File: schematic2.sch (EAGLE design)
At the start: 76 parts, among them IC6 DS3231/SO

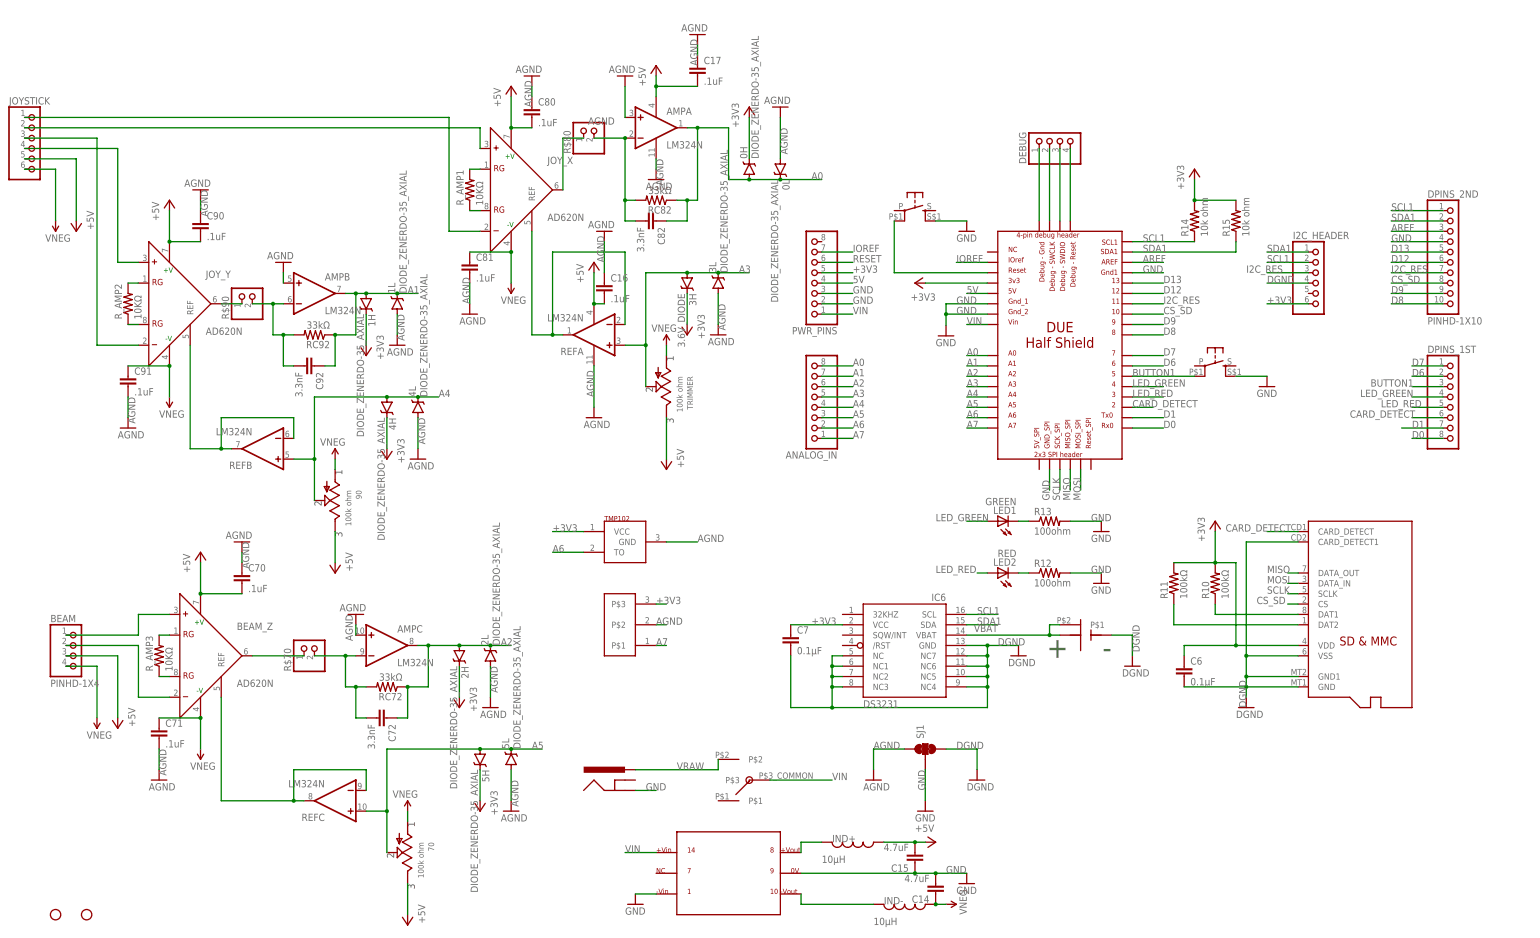
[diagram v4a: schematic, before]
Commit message: Added three separate ground pours for DGND, AGND, and GND.
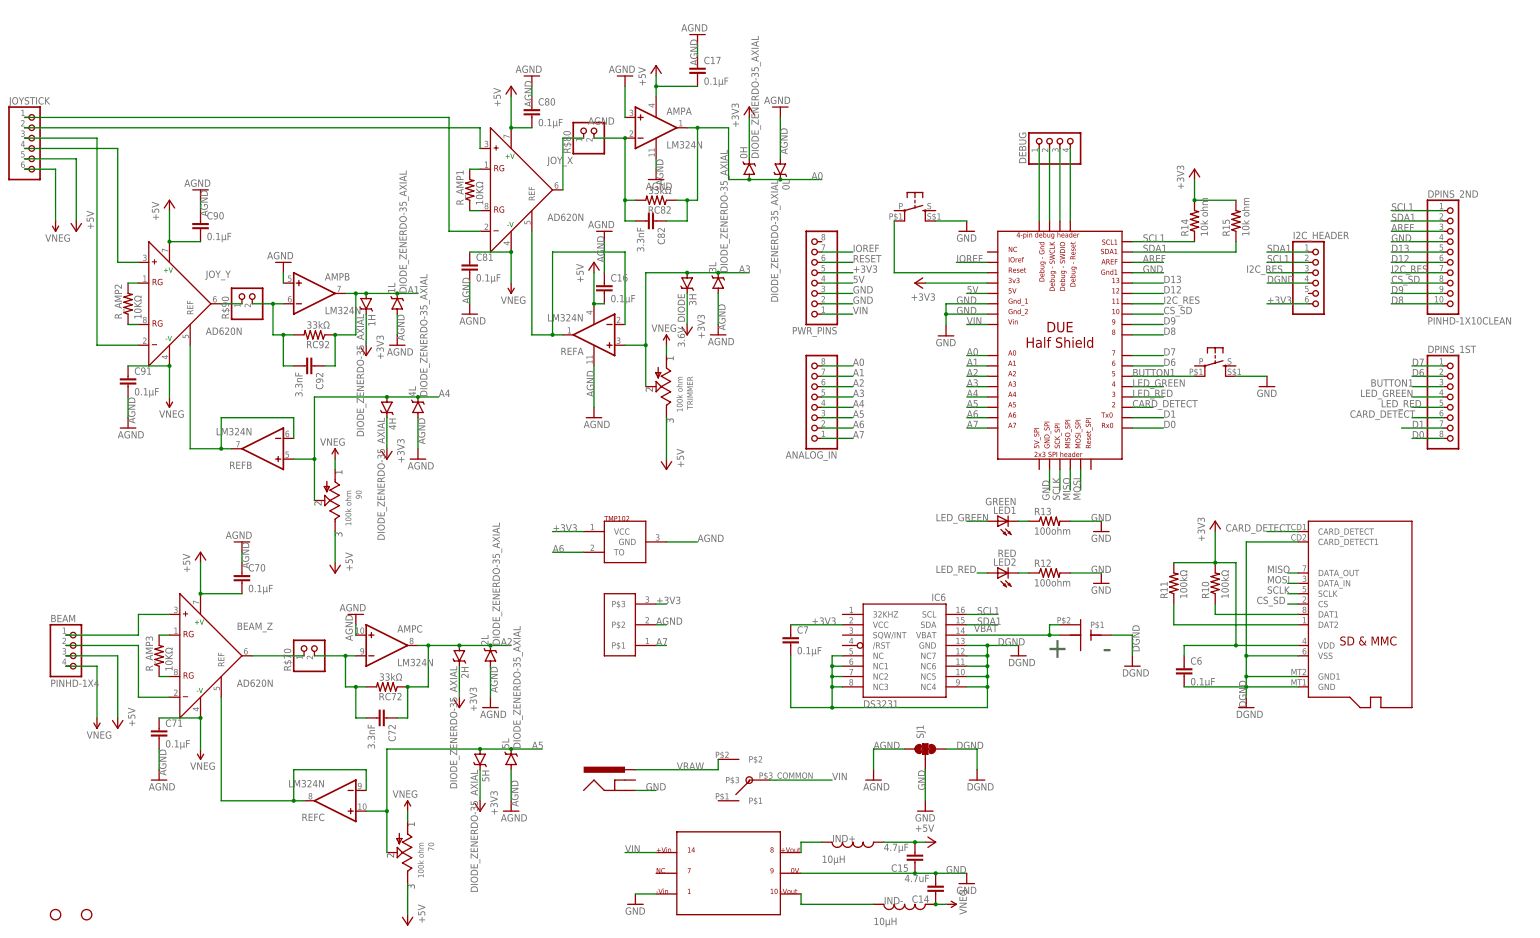
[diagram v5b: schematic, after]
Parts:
- C15: value 4.7uF -> 4.7µF
- C16, C17, C70, C71, C80, C81, C90, C91: value .1uF -> 0.1µF
- DPINS_2ND: value PINHD-1X10 -> PINHD-1X10CLEAN; device Felicia_force_logger:PINHD-1X10 -> Felicia_force_logger:PINHD-1X10CLEAN
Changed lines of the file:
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@@
 <grid distance="0.1" unitdist="inch" unit="inch" style="lines" multiple="1" display="no" altdistance="0.01" altunitdist="inch" altunit="inch"/>
 <layers>
-<layer number="1" name="Top" color="4" fill="1" visible="no" active="no"/>
-<layer number="16" name="Bottom" color="1" fill="1" visible="no" active="no"/>
-<layer number="17" name="Pads" color="2" fill="1" visible="no" active="no"/>
-<layer number="18" name="Vias" color="2" fill="1" visible="no" active="no"/>
-<layer number="19" name="Unrouted" color="6" fill="1" visible="no" active="no"/>
-<layer number="20" name="Dimension" color="15" fill="1" visible="no" active="no"/>
-<layer number="21" name="tPlace" color="7" fill="1" visible="no" active="no"/>
-<layer number="22" name="bPlace" color="7" fill="1" visible="no" active="no"/>
-<layer number="23" name="tOrigins" color="15" fill="1" visible="no" active="no"/>
-<layer number="24" name="bOrigins" color="15" fill="1" visible="no" active="no"/>
-<layer number="25" name="tNames" color="7" fill="1" visible="no" active="no"/>
-<layer number="26" name="bNames" color="7" fill="1" visible="no" active="no"/>
-<layer number="27" name="tValues" color="7" fill="1" visible="no" active="no"/>
-<layer number="28" name="bValues" color="7" fill="1" visible="no" active="no"/>
+<layer number="1" name="Top" color="4" fill="1" visible="yes" active="no"/>
+<layer number="16" name="Bottom" color="1" fill="1" visible="yes" active="no"/>
+<layer number="17" name="Pads" color="2" fill="1" visible="yes" active="no"/>
+<layer number="18" name="Vias" color="2" fill="1" visible="yes" active="no"/>
+<layer number="19" name="Unrouted" color="6" fill="1" visible="yes" active="no"/>
+<layer number="20" name="Dimension" color="15" fill="1" visible="yes" active="no"/>
+<layer number="21" name="tPlace" color="16" fill="1" visible="yes" active="no"/>
+<layer number="22" name="bPlace" color="14" fill="1" visible="yes" active="no"/>
+<layer number="23" name="tOrigins" color="15" fill="1" visible="yes" active="no"/>
+<layer number="24" name="bOrigins" color="15" fill="1" visible="yes" active="no"/>
+<layer number="25" name="tNames" color="7" fill="1" visible="yes" active="no"/>
+<layer number="26" name="bNames" color="7" fill="1" visible="yes" active="no"/>
+<layer number="27" name="tValues" color="7" fill="1" visible="yes" active="no"/>
+<layer number="28" name="bValues" color="7" fill="1" visible="yes" active="no"/>
 <layer number="29" name="tStop" color="7" fill="3" visible="no" active="no"/>
 <layer number="30" name="bStop" color="7" fill="6" visible="no" active="no"/>
@@
 <layer number="35" name="tGlue" color="7" fill="4" visible="no" active="no"/>
 <layer number="36" name="bGlue" color="7" fill="5" visible="no" active="no"/>
-<layer number="37" name="tTest" color="7" fill="1" visible="no" active="no"/>
-<layer number="38" name="bTest" color="7" fill="1" visible="no" active="no"/>
+<layer number="37" name="tTest" color="7" fill="1" visible="yes" active="no"/>
+<layer number="38" name="bTest" color="7" fill="1" visible="yes" active="no"/>
 <layer number="39" name="tKeepout" color="4" fill="11" visible="no" active="no"/>
 <layer number="40" name="bKeepout" color="1" fill="11" visible="no" active="no"/>
@@
 <layer number="44" name="Drills" color="7" fill="1" visible="no" active="no"/>
 <layer number="45" name="Holes" color="7" fill="1" visible="no" active="no"/>
-<layer number="46" name="Milling" color="3" fill="1" visible="no" active="no"/>
-<layer number="47" name="Measures" color="7" fill="1" visible="no" active="no"/>
-<layer number="48" name="Document" color="7" fill="1" visible="no" active="no"/>
-<layer number="49" name="Reference" color="7" fill="1" visible="no" active="no"/>
-<layer number="50" name="dxf" color="7" fill="1" visible="no" active="no"/>
-<layer number="51" name="tDocu" color="7" fill="1" visible="no" active="no"/>
-<layer number="52" name="bDocu" color="7" fill="1" visible="no" active="no"/>
-<layer number="53" name="tGND_GNDA" color="7" fill="9" visible="no" active="no"/>
-<layer number="54" name="bGND_GNDA" color="1" fill="9" visible="no" active="no"/>
-<layer number="56" name="wert" color="7" fill="1" visible="no" active="no"/>
-<layer number="57" name="tCAD" color="7" fill="1" visible="no" active="no"/>
+<layer number="46" name="Milling" color="3" fill="1" visible="yes" active="no"/>
+<layer number="47" name="Measures" color="7" fill="1" visible="yes" active="no"/>
+<layer number="48" name="Document" color="7" fill="1" visible="yes" active="no"/>
+<layer number="49" name="Reference" color="7" fill="1" visible="yes" active="no"/>
+<layer number="50" name="dxf" color="7" fill="1" visible="yes" active="no"/>
+<layer number="51" name="tDocu" color="6" fill="1" visible="yes" active="no"/>
+<layer number="52" name="bDocu" color="7" fill="1" visible="yes" active="no"/>
+<layer number="53" name="tGND_GNDA" color="7" fill="9" visible="yes" active="no"/>
+<layer number="54" name="bGND_GNDA" color="1" fill="9" visible="yes" active="no"/>
+<layer number="56" name="wert" color="7" fill="1" visible="yes" active="no"/>
+<layer number="57" name="tCAD" color="7" fill="1" visible="yes" active="no"/>
 <layer number="90" name="Modules" color="5" fill="1" visible="yes" active="yes"/>
 <layer number="91" name="Nets" color="2" fill="1" visible="yes" active="yes"/>
@@
 <part name="P-9" library="Felicia_force_logger" deviceset="VNEG" device=""/>
 <part name="P+9" library="supply1" deviceset="+5V" device=""/>
-<part name="C15" library="Felicia_force_logger" deviceset="CAP" device="0805" value="4.7uF"/>
+<part name="C15" library="Felicia_force_logger" deviceset="CAP" device="0805" value="4.7µF"/>
 <part name="C14" library="Felicia_force_logger" deviceset="CAP" device="0805" value="4.7uF"/>
 <part name="IND+" library="Felicia_force_logger" deviceset="INDUCTOR" device="0805_TY" value="10µH"/>
@@
 <part name="R$70" library="Felicia_force_logger" deviceset="PINHD-1X2" device=""/>
 <part name="DPINS_1ST" library="Felicia_force_logger" deviceset="PINHD-1X8" device="CLEANBIG"/>
-<part name="DPINS_2ND" library="Felicia_force_logger" deviceset="PINHD-1X10" device=""/>
+<part name="DPINS_2ND" library="Felicia_force_logger" deviceset="PINHD-1X10" device="CLEAN" value="PINHD-1X10CLEAN"/>
 <part name="ANALOG_IN" library="Felicia_force_logger" deviceset="PINHD-1X8" device="CLEANBIG"/>
 <part name="PWR_PINS" library="Felicia_force_logger" deviceset="PINHD-1X8" device="CLEANBIG"/>
 <part name="TMP102" library="Felicia_force_logger" deviceset="LM62" device=""/>
-<part name="C90" library="Felicia_force_logger" deviceset="CAP" device="0805" value=".1uF"/>
-<part name="C91" library="Felicia_force_logger" deviceset="CAP" device="0805" value=".1uF"/>
-<part name="C80" library="Felicia_force_logger" deviceset="CAP" device="0805" value=".1uF"/>
-<part name="C81" library="Felicia_force_logger" deviceset="CAP" device="0805" value=".1uF"/>
-<part name="C70" library="Felicia_force_logger" deviceset="CAP" device="0805" value=".1uF"/>
-<part name="C71" library="Felicia_force_logger" deviceset="CAP" device="0805" value=".1uF"/>
-<part name="C16" library="Felicia_force_logger" deviceset="CAP" device="0805" value=".1uF"/>
+<part name="C90" library="Felicia_force_logger" deviceset="CAP" device="0805" value="0.1µF"/>
+<part name="C91" library="Felicia_force_logger" deviceset="CAP" device="0805" value="0.1µF"/>
+<part name="C80" library="Felicia_force_logger" deviceset="CAP" device="0805" value="0.1µF"/>
+<part name="C81" library="Felicia_force_logger" deviceset="CAP" device="0805" value="0.1µF"/>
+<part name="C70" library="Felicia_force_logger" deviceset="CAP" device="0805" value="0.1µF"/>
+<part name="C71" library="Felicia_force_logger" deviceset="CAP" device="0805" value="0.1µF"/>
+<part name="C16" library="Felicia_force_logger" deviceset="CAP" device="0805" value="0.1µF"/>
 <part name="P+10" library="supply1" deviceset="+5V" device=""/>
 <part name="GND26" library="Felicia_force_logger" deviceset="AGND" device=""/>
-<part name="C17" library="Felicia_force_logger" deviceset="CAP" device="0805" value=".1uF"/>
+<part name="C17" library="Felicia_force_logger" deviceset="CAP" device="0805" value="0.1µF"/>
 <part name="P+11" library="supply1" deviceset="+5V" device=""/>
 <part name="GND27" library="Felicia_force_logger" deviceset="AGND" device=""/>

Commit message: Renamed a bunch of the resistors and capacitors so that they are in a more sensible order on the board.
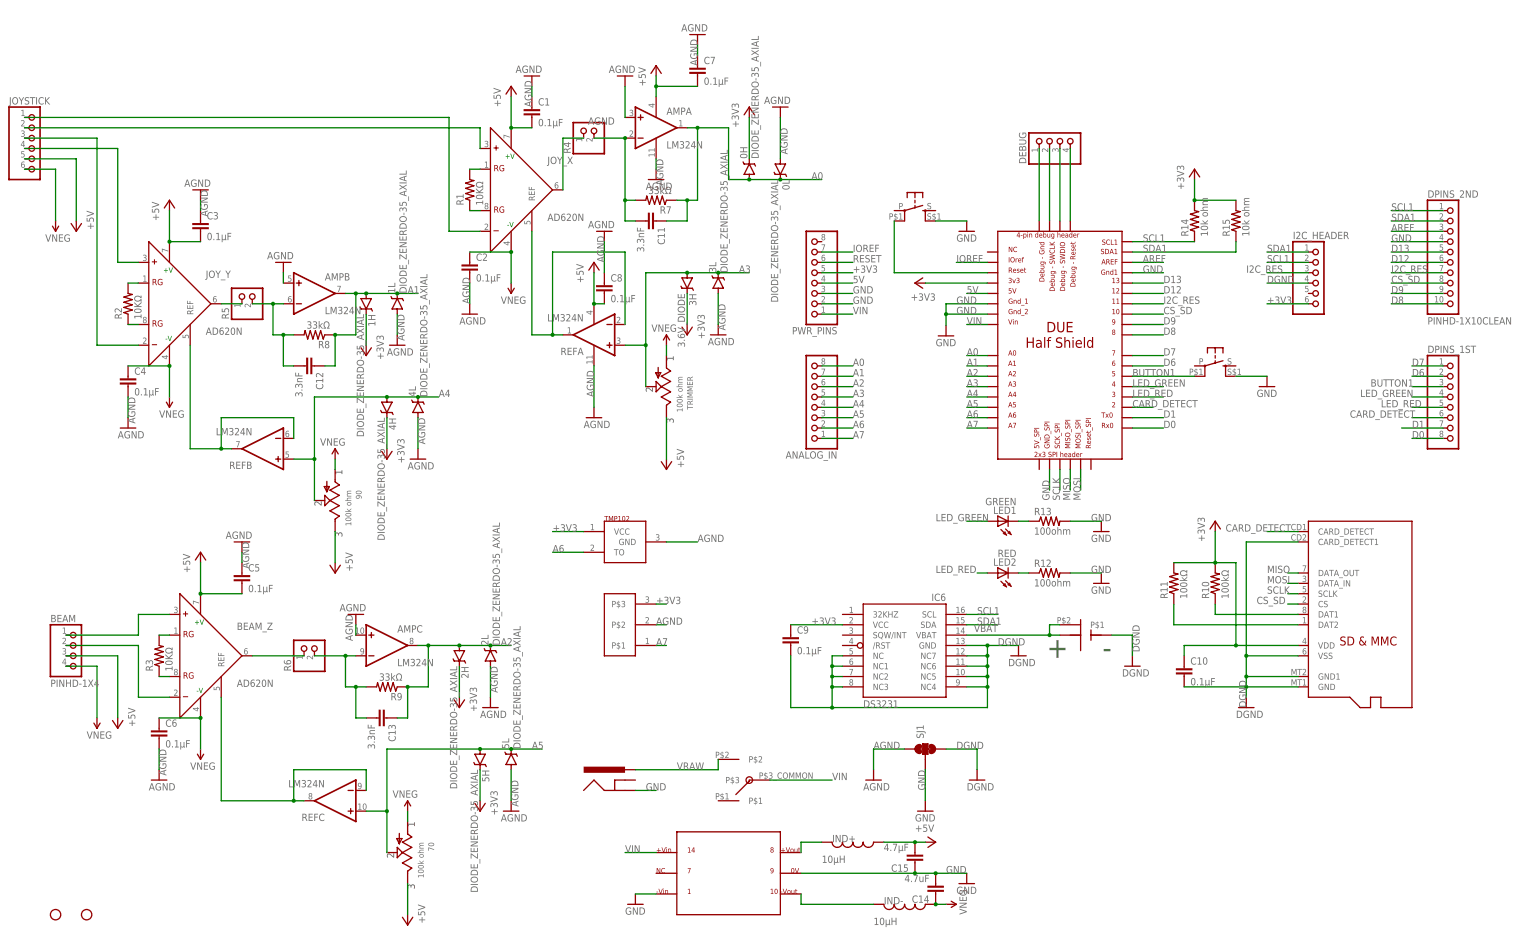
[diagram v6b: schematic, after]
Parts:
- removed C17, C71: 0.1µF, Felicia_force_logger:CAP0805
- added C10, C9: 0.1µF, Felicia_force_logger:CAP0805
- renumbered C16 to C8, C70 to C5, C72 to C13, C80 to C1, C81 to C2, C82 to C11, C90 to C3, C91 to C4, C92 to C12, R$70 to R6, R$80 to R4, R$90 to R5, RC72 to R9, RC82 to R7, RC92 to R8, R_AMP1 to R1, R_AMP2 to R2, R_AMP3 to R3
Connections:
- net +3V3: now also C10.1, C9.1; no longer C6.1, C7.1
- net +5V: now also C7.2; no longer C17.2
- net AGND: now also C6.2, C7.1; no longer C17.1, C71.2
- net DGND: now also C10.2, C9.2; no longer C6.2, C7.2
- net VNEG: now also C6.1; no longer C71.1
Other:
- moved on the sheet: C6, C7
